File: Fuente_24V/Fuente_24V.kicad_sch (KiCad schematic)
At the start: 0 parts

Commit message: Se agrega el esquemático y pcb de Fuente
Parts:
- added F1: Fuse, Fuse:Fuseholder_Cylinder-5x20mm_Schurter_0031_8201_Horizontal_Open, symbol Device:Fuse
- added H1, H2, H3, H4: MountingHole_2.2mm_M2_ISO7380_Pad, MountingHole:MountingHole_2.2mm_M2_ISO7380_Pad, symbol Mechanical:MountingHole_Pad
- added J1: Screw_Terminal_01x03, TerminalBlock:TerminalBlock_MaiXu_MX126-5.0-03P_1x03_P5.00mm, symbol Connector:Screw_Terminal_01x03
- added J2: Screw_Terminal_01x02, TerminalBlock:TerminalBlock_MaiXu_MX126-5.0-02P_1x02_P5.00mm, symbol Connector:Screw_Terminal_01x02
- added PS1, PS2: HLK-5M12, Converter_ACDC:Converter_ACDC_Hi-Link_HLK-5Mxx, symbol Converter_ACDC:HLK-5M12
- added RV1: Varistor, Varistor:RV_Disc_D12mm_W4mm_P7.5mm, symbol Device:Varistor
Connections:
- new net: F1.2, PS1.1 (AC/L), PS2.1 (AC/L), RV1.1
- new net: J1.2 (Pin_2), PS1.2 (AC/N), PS2.2 (AC/N), RV1.2
- new net: PS1.3 (-Vout), PS2.4 (+Vout)
- new net: F1.1, J1.1 (Pin_1)
- new net +24V: J2.1 (Pin_1), PS1.4 (+Vout)
- new net Earth: J1.3 (Pin_3)
- new net GND: J2.2 (Pin_2), PS2.3 (-Vout)
- no-connect marks 0 -> 4
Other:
- company: (none) -> Labtel
- title: (none) -> Fuente 24 Volt

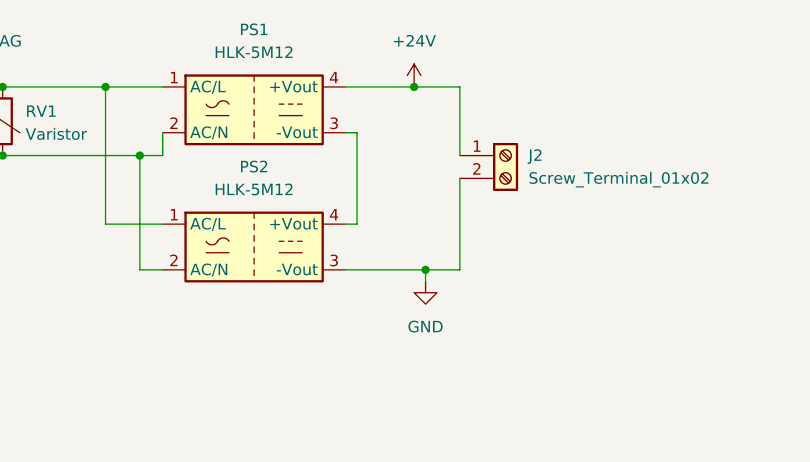
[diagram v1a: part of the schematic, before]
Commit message: se agrega led indicador de fuente al esquema
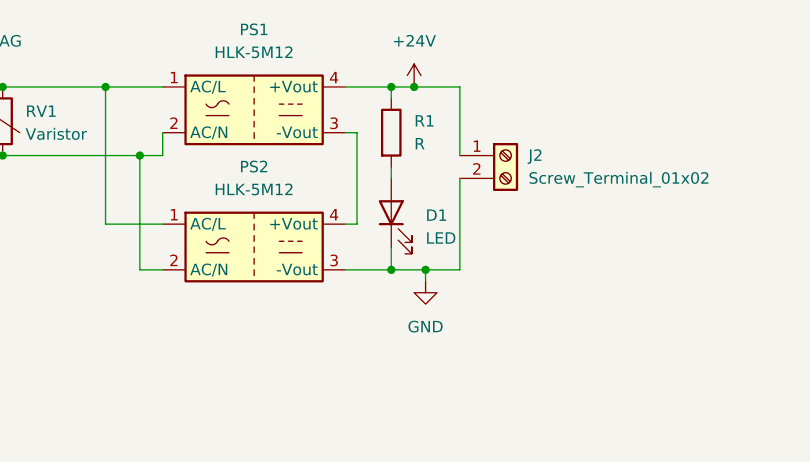
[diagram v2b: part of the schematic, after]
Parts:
- added D1: LED, LED_THT:LED_D3.0mm, symbol Device:LED
- added R1: R, Resistor_THT:R_Axial_DIN0207_L6.3mm_D2.5mm_P10.16mm_Horizontal, symbol Device:R
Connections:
- net +24V: now also R1.1
- net GND: now also D1.1 (K)
- new net: D1.2 (A), R1.2
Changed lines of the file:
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@@
+	)
+	(junction
+		(at 168.91 100.33)
+		(diameter 0)
+		(color 0 0 0 0)
 	)
 	(junction
@@
 	)
 	(junction
+		(at 168.91 80.01)
+		(diameter 0)
+		(color 0 0 0 0)
+	)
+	(junction
 		(at 107.95 80.01)
 		(diameter 0)
@@
 	(wire
 		(pts
+			(xy 168.91 100.33) (xy 163.83 100.33)
+		)
+		(stroke
+			(width 0)
+			(type default)
+		)
+	)
+	(wire
+		(pts
 			(xy 120.65 80.01) (xy 123.19 80.01)
 		)
@@
 	(wire
 		(pts
-			(xy 163.83 80.01) (xy 171.45 80.01)
+			(xy 163.83 80.01) (xy 168.91 80.01)
 		)
 		(stroke
@@
 	(wire
 		(pts
+			(xy 168.91 80.01) (xy 168.91 81.28)
+		)
+		(stroke
+			(width 0)
+			(type default)
+		)
+	)
+	(wire
+		(pts
 			(xy 176.53 80.01) (xy 176.53 87.63)
 		)
@@
 	(wire
 		(pts
+			(xy 168.91 80.01) (xy 171.45 80.01)
+		)
+		(stroke
+			(width 0)
+			(type default)
+		)
+	)
+	(wire
+		(pts
 			(xy 110.49 82.55) (xy 118.11 82.55)
 		)
@@
 	(wire
 		(pts
+			(xy 168.91 97.79) (xy 168.91 100.33)
+		)
+		(stroke
+			(width 0)
+			(type default)
+		)
+	)
+	(wire
+		(pts
 			(xy 176.53 100.33) (xy 172.72 100.33)
 		)
@@
 	(wire
 		(pts
+			(xy 168.91 88.9) (xy 168.91 90.17)
+		)
+		(stroke
+			(width 0)
+			(type default)
+		)
+	)
+	(wire
+		(pts
 			(xy 140.97 100.33) (xy 140.97 87.63)
 		)
@@
 	(wire
 		(pts
-			(xy 172.72 100.33) (xy 163.83 100.33)
+			(xy 172.72 100.33) (xy 168.91 100.33)
 		)
 		(stroke
@@
 	)
 	(symbol
+		(lib_id "Device:R")
+		(at 168.91 85.09 0)
+		(unit 1)
+		(exclude_from_sim no)
+		(in_bom yes)
+		(on_board yes)
+		(dnp no)
+		(fields_autoplaced yes)
+		(property "Reference" "R1"
+			(at 171.45 83.8199 0)
+			(effects
+				(font
+					(size 1.27 1.27)
+				)
+				(justify left)
+			)
+		)
+		(property "Value" "R"
+			(at 171.45 86.3599 0)
+			(effects
+				(font
+					(size 1.27 1.27)
+				)
+				(justify left)
+			)
+		)
+		(property "Footprint" "Resistor_THT:R_Axial_DIN0207_L6.3mm_D2.5mm_P10.16mm_Horizontal"
+			(at 167.132 85.09 90)
+			(effects
+				(font
+					(size 1.27 1.27)
+				)
+				(hide yes)
+			)
+		)
+		(property "Datasheet" "~"
+			(at 168.91 85.09 0)
+			(effects
+				(font
+					(size 1.27 1.27)
+				)
+				(hide yes)
+			)
+		)
+		(property "Description" "Resistor"
+			(at 168.91 85.09 0)
+			(effects
+				(font
+					(size 1.27 1.27)
+				)
+				(hide yes)
+			)
+		)
+		(pin "1"
+		)
+		(pin "2"
+		)
+		(instances
+			(project ""
+				(path "/3efc57b9-147f-483f-982a-3723e51cac7c"
+					(reference "R1")
+					(unit 1)
+				)
+			)
+		)
+	)
+	(symbol
 		(lib_id "Device:Varistor")
 		(at 125.73 83.82 0)
@@
 					(unit 1)
 				)
+			)
+		)
+	)
+	(symbol
+		(lib_id "Device:LED")
+		(at 168.91 93.98 90)
+		(unit 1)
+		(exclude_from_sim no)
+		(in_bom yes)
+		(on_board yes)
+		(dnp no)
+		(fields_autoplaced yes)
+		(property "Reference" "D1"
+			(at 172.72 94.2974 90)
+			(effects
+				(font
+					(size 1.27 1.27)
+				)
+				(justify right)
+			)
+		)
+		(property "Value" "LED"
+			(at 172.72 96.8374 90)
+			(effects
+				(font
+					(size 1.27 1.27)
+				)
+				(justify right)
+			)
+		)
+		(property "Footprint" "LED_THT:LED_D3.0mm"
+			(at 168.91 93.98 0)
+			(effects
+				(font
+					(size 1.27 1.27)
+				)
+				(hide yes)
+			)
+		)
+		(property "Datasheet" "~"
+			(at 168.91 93.98 0)
+			(effects
+				(font
+					(size 1.27 1.27)
+				)
+				(hide yes)
+			)
+		)
+		(property "Description" "Light emitting diode"
+			(at 168.91 93.98 0)
+			(effects
+				(font
+					(size 1.27 1.27)
+				)
+				(hide yes)
+			)
+		)
+		(property "Sim.Pins" "1=K 2=A"
+			(at 168.91 93.98 0)
+			(effects
+				(font
+					(size 1.27 1.27)
+				)
+				(hide yes)
+			)
+		)
+		(pin "1"
+		)
+		(pin "2"
+		)
+		(instances
+			(project ""
+				(path "/3efc57b9-147f-483f-982a-3723e51cac7c"
+					(reference "D1")
+					(unit 1)
+				)
